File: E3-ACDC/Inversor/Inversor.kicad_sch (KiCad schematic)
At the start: 8 parts, among them Q1 IRF840A, Q2 IRF840A, U2 TL494

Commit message: Added the first part of inverter
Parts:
- added R7, R8: 10k, Resistor_THT:R_Axial_DIN0207_L6.3mm_D2.5mm_P2.54mm_Vertical, symbol PCM_Resistor_AKL:R_0201
- R6: value 3.3k -> 2k
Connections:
- net GND: now also U2.1 (1IN+), U2.10 (E2), U2.16 (2IN+), U2.3 (FB), U2.9 (E1)
- net PWM_H: now also U2.8 (C1), R7.1; no longer U2.9 (E1)
- net PWM_L: now also U2.11 (C2), R8.1; no longer U2.10 (E2)
- net REF: no longer U2.1 (1IN+), U2.16 (2IN+)
- removed net 9V: U2.11 (C2), U2.12 (VCC), U2.8 (C1)
- new net 12V: R7.2, R8.2, U2.12 (VCC)

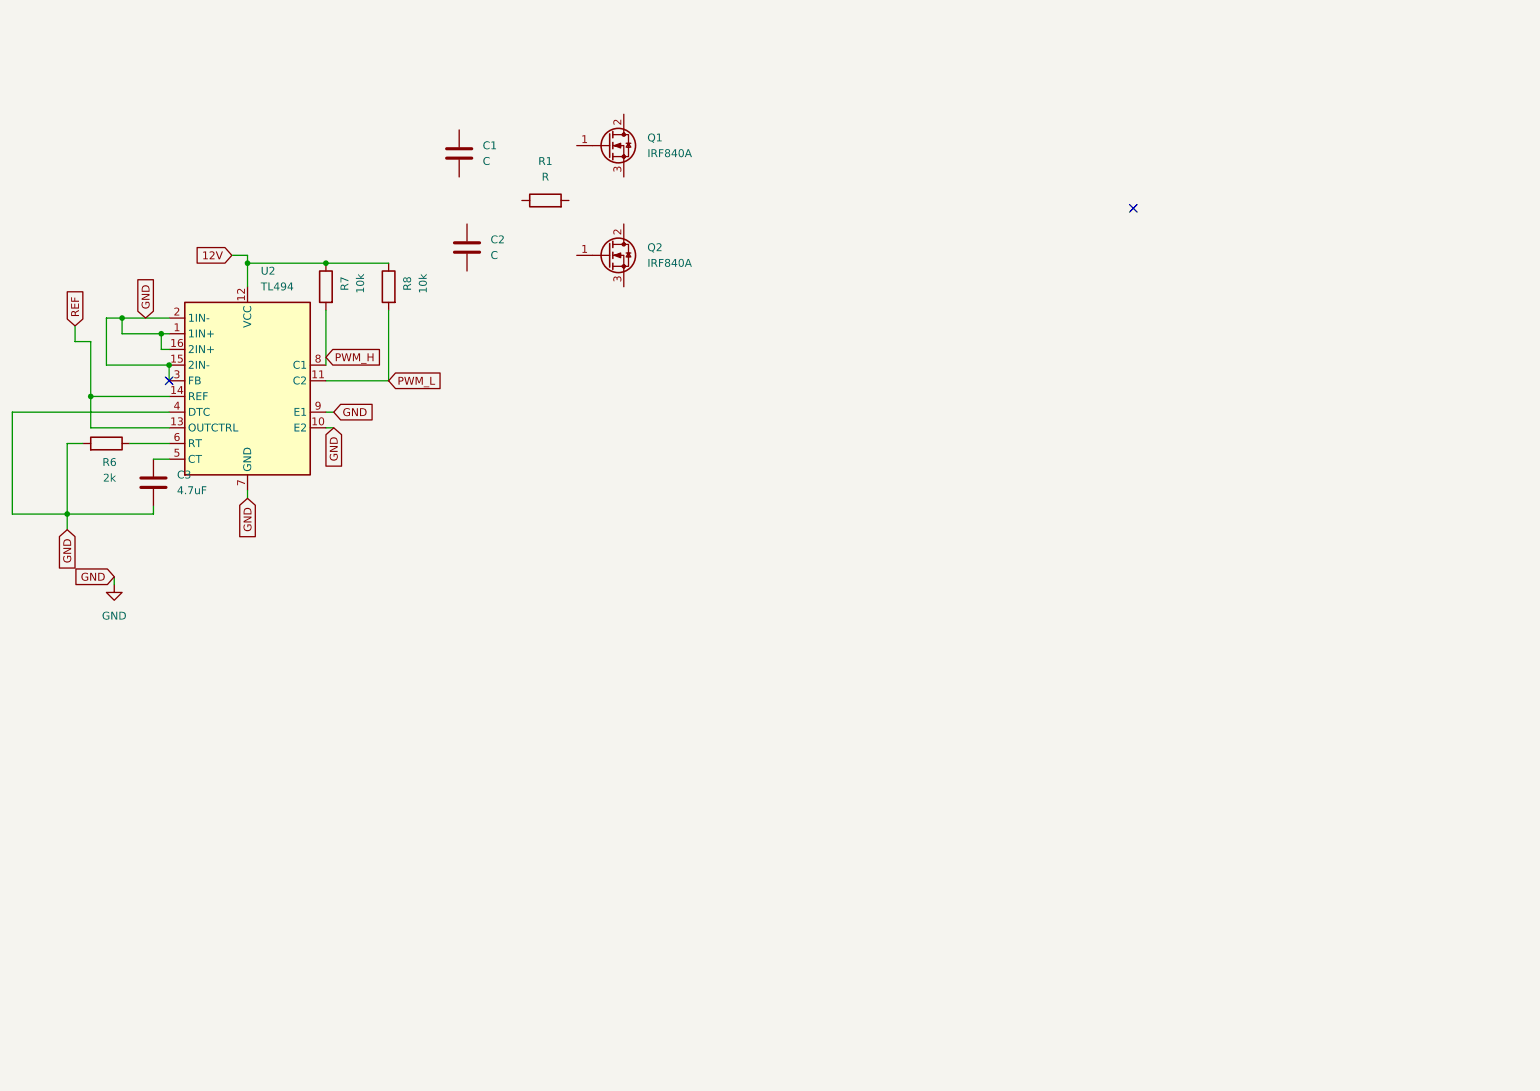
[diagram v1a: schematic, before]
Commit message: Updated Inversor Schematic
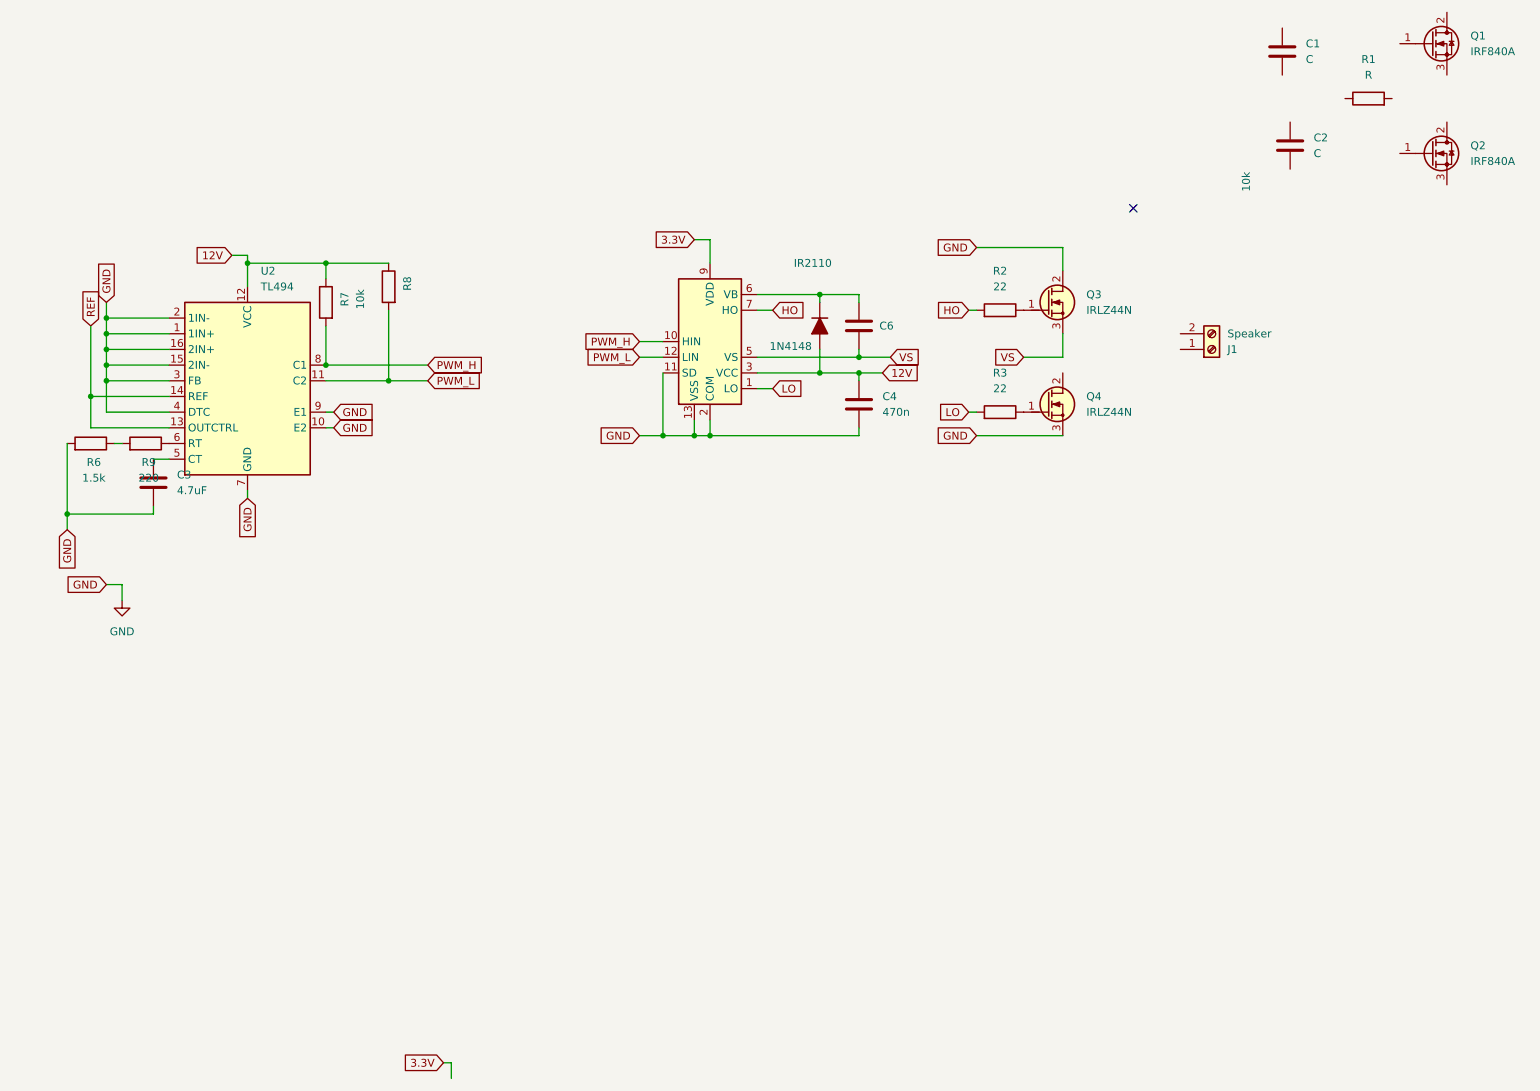
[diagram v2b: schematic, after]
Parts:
- added C4, C6: 470n, Capacitor_THT:C_Disc_D3.8mm_W2.6mm_P2.50mm, symbol PCM_Capacitor_AKL:C_0201
- added D1: 1N4148, PCM_Diode_THT_AKL:D_DO-35_SOD27_P7.62mm_Horizontal, symbol PCM_Diode_AKL:1N4148
- added J1: Speaker, TerminalBlock:TerminalBlock_MaiXu_MX126-5.0-02P_1x02_P5.00mm, symbol Connector:Screw_Terminal_01x02
- added Q3, Q4: IRLZ44N, PCM_Package_TO_SOT_THT_AKL:TO-220-3_Vertical_GDS, symbol PCM_Transistor_MOSFET_AKL:IRLZ44N
- added R2, R3: 22, Resistor_THT:R_Axial_DIN0204_L3.6mm_D1.6mm_P7.62mm_Horizontal, symbol PCM_Resistor_AKL:R_0201
- added R9: 220, Resistor_THT:R_Axial_DIN0207_L6.3mm_D2.5mm_P2.54mm_Vertical, symbol PCM_Resistor_AKL:R_0201
- added U1: IR2110, Package_DIP:DIP-14_W7.62mm, symbol Driver_FET:IR2110
- R6: value 2k -> 1.5k
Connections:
- net 12V: now also C4.1, D1.2 (A), U1.3 (VCC)
- net GND: now also C4.2, Q3.2 (D), Q4.3 (S), U1.11 (SD), U1.13 (VSS), U1.2 (COM)
- net PWM_H: now also U1.10 (HIN)
- net PWM_L: now also U1.12 (LIN)
- net at R6.2: now also R9.1; no longer U2.6 (RT)
- new net: R9.2, U2.6 (RT)
- new net: C6.1, D1.1 (K), U1.6 (VB)
- new net: Q4.1 (G), R3.2
- new net: Q3.1 (G), R2.2
- new net 3.3V: U1.9 (VDD)
- new net HO: R2.1, U1.7 (HO)
- new net LO: R3.1, U1.1 (LO)
- new net VS: C6.2, Q3.3 (S), U1.5 (VS)
- no-connect marks 2 -> 1
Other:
- moved on the sheet: C1, C2, Q1, Q2, R1, R6, R7

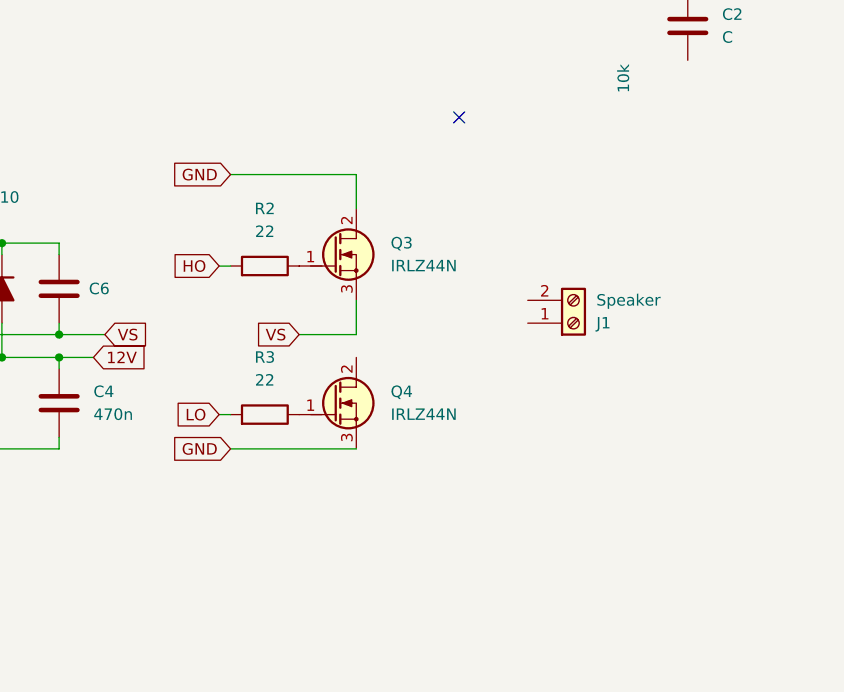
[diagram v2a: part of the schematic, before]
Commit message: Changed MOSFET Polarity
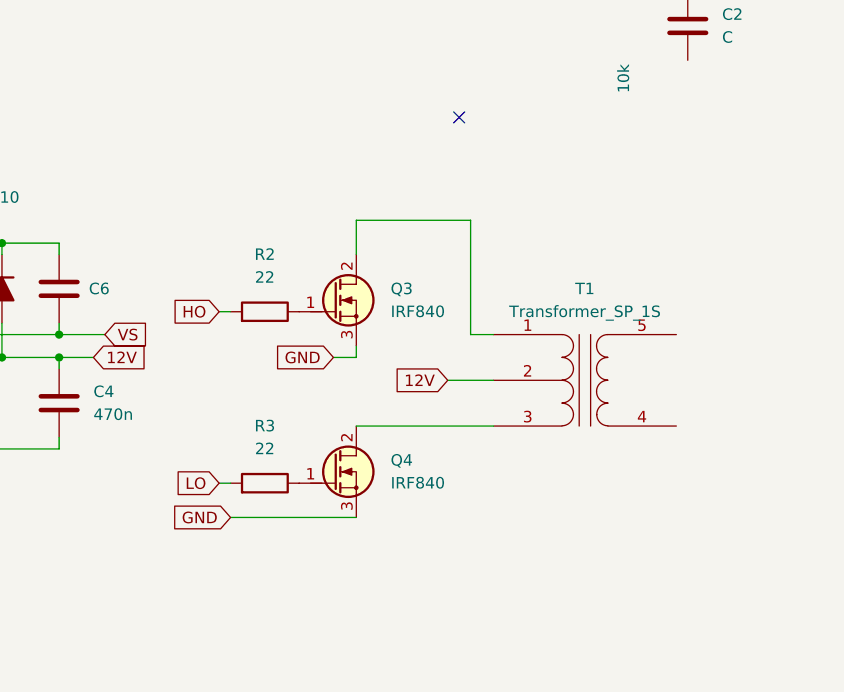
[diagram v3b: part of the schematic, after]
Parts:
- removed J1: Speaker, TerminalBlock:TerminalBlock_MaiXu_MX126-5.0-02P_1x02_P5.00mm, symbol Connector:Screw_Terminal_01x02
- added T1: Transformer_SP_1S, symbol Device:Transformer_SP_1S
- Q3, Q4: value IRLZ44N -> IRF840
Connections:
- net 12V: now also T1.2 (PM)
- net GND: now also Q3.3 (S); no longer Q3.2 (D)
- net VS: no longer Q3.3 (S)
- net at Q4.2 (D): now also T1.3 (PR2)
- new net: Q3.2 (D), T1.1 (PR1)
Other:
- moved on the sheet: Q3, Q4, R2, R3

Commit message: Ended Inversor Schematic
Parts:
- removed C1, C2: C, symbol Device:C
- removed C3: 4.7uF, Capacitor_THT:CP_Radial_D10.0mm_P3.50mm, symbol PCM_Capacitor_AKL:C_Rect_L26.5mm_W8.5mm_P22.50mm
- removed C6: 470n, Capacitor_THT:C_Disc_D3.8mm_W2.6mm_P2.50mm, symbol PCM_Capacitor_AKL:C_0201
- removed D1: 1N4148, PCM_Diode_THT_AKL:D_DO-35_SOD27_P7.62mm_Horizontal, symbol PCM_Diode_AKL:1N4148
- removed Q1, Q2: IRF840A, Package_TO_SOT_THT:TO-220-3_Vertical, symbol Transistor_FET:IRF840A
- removed R1: R, symbol Device:R
- removed R6: 1.5k, Resistor_THT:R_Axial_DIN0207_L6.3mm_D2.5mm_P2.54mm_Vertical, symbol PCM_Resistor_AKL:R_0201
- removed R7, R8: 10k, Resistor_THT:R_Axial_DIN0207_L6.3mm_D2.5mm_P2.54mm_Vertical, symbol PCM_Resistor_AKL:R_0201
- removed R9: 220, Resistor_THT:R_Axial_DIN0207_L6.3mm_D2.5mm_P2.54mm_Vertical, symbol PCM_Resistor_AKL:R_0201
- removed U2: TL494, PCM_Package_DIP_AKL:DIP-16_W7.62mm_Socket_LongPads, symbol Regulator_Controller:TL494
- added J4, J5: Conn_01x20_Socket, Connector_PinHeader_2.54mm:PinHeader_1x20_P2.54mm_Vertical, symbol Connector:Conn_01x20_Socket
- C4: value 470n -> 10u
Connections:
- net VS is gone; now on net GND: U1.5 (VS)
- net 12V: now also U1.6 (VB); no longer T1.2 (PM)
- net 3.3V: now also J4.18 (Pin_18)
- net GND: now also J4.19 (Pin_19)
- net PWM_H renamed A8 PWM_H
- net A8 PWM_H: now also J5.5 (Pin_5)
- net PWM_L renamed A7 PWM_L
- net A7 PWM_L: now also J4.13 (Pin_13)
- new net 6V: T1.2 (PM)
- new net A0: J4.6 (Pin_6)
- new net A1: J4.7 (Pin_7)
- new net A10: J5.7 (Pin_7)
- new net A9: J5.6 (Pin_6)
- new net B0: J4.14 (Pin_14)
- new net B1: J4.15 (Pin_15)
- new net B10: J4.17 (Pin_17)
- new net B2: J4.16 (Pin_16)
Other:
- note added: "STLINK"
- moved on the sheet: C4
